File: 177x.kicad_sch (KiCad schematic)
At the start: 11 parts, among them IC1 WD1770, IC2 74HCT00, IC3 74HCT173, IC4 74HCT02, IC5 8271

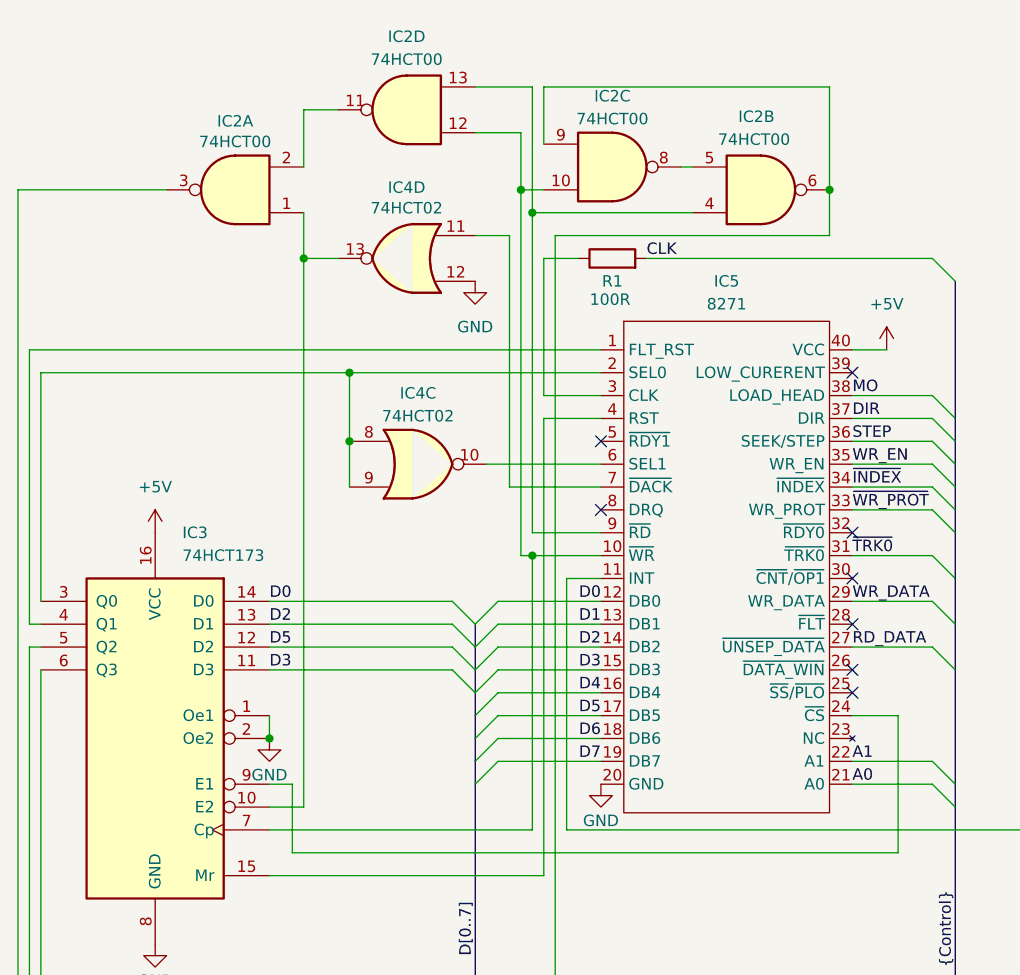
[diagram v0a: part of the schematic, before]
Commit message: Revised PCB layout
PCB dimensions reduced. Overhang now significantly reduced.
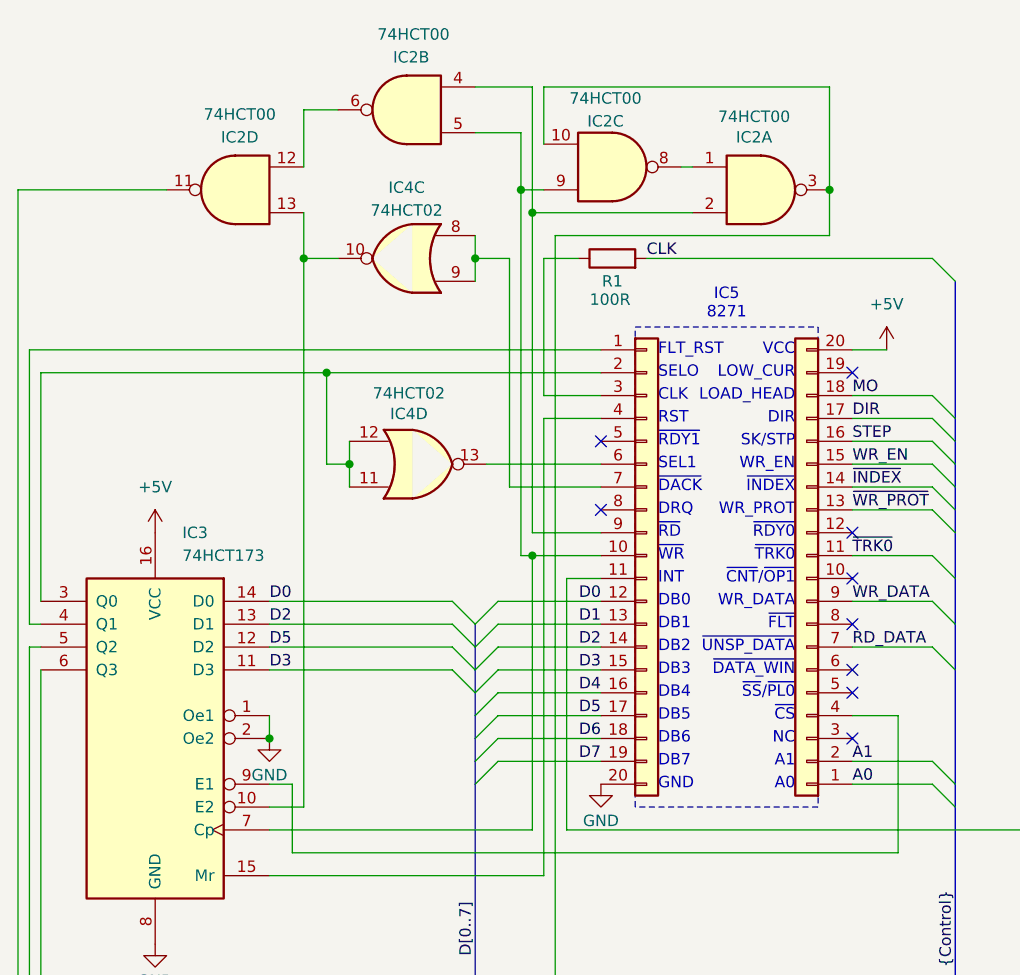
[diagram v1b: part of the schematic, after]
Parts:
- removed IC5: 8271, Package_DIP:DIP-40_W15.24mm, symbol Disc_Library:8271
- added J1: Conn_01x20, 177x_pretty:PinHeader_1_20_P2.54mm_Vertical, symbol Connector_Generic:Conn_01x20
- added J2: Conn_01x20, 177x_pretty:PinHeader_21_40_P2.54mm_Vertical, symbol Connector_Generic:Conn_01x20
- IC1: footprint Package_DIP:DIP-28_W15.24mm -> Package_DIP:DIP-28_W15.24mm_Socket
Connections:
- net +5V: now also J2.20 (Pin_20)
- net A0: now also J2.1 (Pin_1)
- net A1: now also J2.2 (Pin_2)
- net D0: now also J1.12 (Pin_12)
- net D1: now also J1.13 (Pin_13)
- net D2: now also J1.14 (Pin_14)
- net D3: now also J1.15 (Pin_15)
- net D4: now also J1.16 (Pin_16)
- net D5: now also J1.17 (Pin_17)
- net D6: now also J1.18 (Pin_18)
- net D7: now also J1.19 (Pin_19)
- net DIR: now also J2.17 (Pin_17)
- net GND: now also J1.20 (Pin_20); no longer IC4.12
- net MO: now also J2.18 (Pin_18)
- net RD_DATA: now also J2.7 (Pin_7)
- net STEP: now also J2.16 (Pin_16)
- net WR_DATA: now also J2.9 (Pin_9)
- net WR_EN: now also J2.15 (Pin_15)
- net ~{INDEX}: now also J2.14 (Pin_14)
- net ~{TRK0}: now also J2.11 (Pin_11)
- net ~{WR_PROT}: now also J2.13 (Pin_13)
- net at IC4.10: now also IC2.13, IC3.10 (E2)
- net at IC4.8, IC4.9: now also J1.7 (Pin_7); no longer IC3.3 (Q0)
- net at IC2.11: now also IC1.1 (~{CS}); no longer IC2.2
- net at IC2.4: now also IC2.2, J1.9 (Pin_9); no longer IC2.13
- net at IC4.1: now also J1.11 (Pin_11)
- net at IC2.5: now also IC2.9, IC3.7 (Cp), J1.10 (Pin_10); no longer IC2.8
- net at IC2.3: now also IC1.2 (R/~{W}), IC2.10; no longer IC1.1 (~{CS})
- net at R1.1: now also J1.3 (Pin_3)
- net at IC3.15 (Mr): now also J1.4 (Pin_4)
- net at IC3.4 (Q1): now also J1.1 (Pin_1)
- net at IC3.9 (E1): now also J2.4 (Pin_4)
- net at IC4.11: now also IC3.3 (Q0), IC4.12, J1.2 (Pin_2)
- new net: IC2.12, IC2.6
- new net: IC4.13, J1.6 (Pin_6)
- new net: IC2.1, IC2.8
- no-connect marks 8 -> 9
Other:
- note added: "A0"
- note added: "A1"
- note added: "CLK"
- note added: "DB0"
- note added: "DB1"
- note added: "DB2"
- note added: "DB3"
- note added: "DB4"
- note added: "DB5"
- note added: "DB6"
- note added: "DB7"
- note added: "DIR"
- note added: "DRQ"
- note added: "FLT_RST"
- note added: "GND"
- note added: "IC5 8271"
- note added: "INT"
- note added: "LOAD_HEAD"
- note added: "LOW_CUR"
- note added: "NC"
- note added: "RST"
- note added: "SEL1"
- note added: "SELO"
- note added: "SK/STP"
- note added: "VCC"
- note added: "WR_DATA"
- note added: "WR_EN"
- note added: "WR_PROT"
- note added: "~{CNT}/~{OP1}"
- note added: "~{CS}"
- note added: "~{DACK}"
- note added: "~{DATA_WIN}"
- note added: "~{FLT}"
- note added: "~{INDEX}"
- note added: "~{RDY0}"
- note added: "~{RDY1}"
- note added: "~{RD}"
- note added: "~{SS}/~{PL0}"
- note added: "~{TRK0}"
- note added: "~{UNSP_DATA}"
- note added: "~{WR}"
- title: Model B - 1770 Disc Interface -> BBC Model B - 177x Disc Interface
- moved on the sheet: IC2A, IC2B, IC2D, IC4C, IC4D
